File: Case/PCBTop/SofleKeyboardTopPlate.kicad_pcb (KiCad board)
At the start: 2 copper layers, 137.2 x 109.2 mm, 5 parts

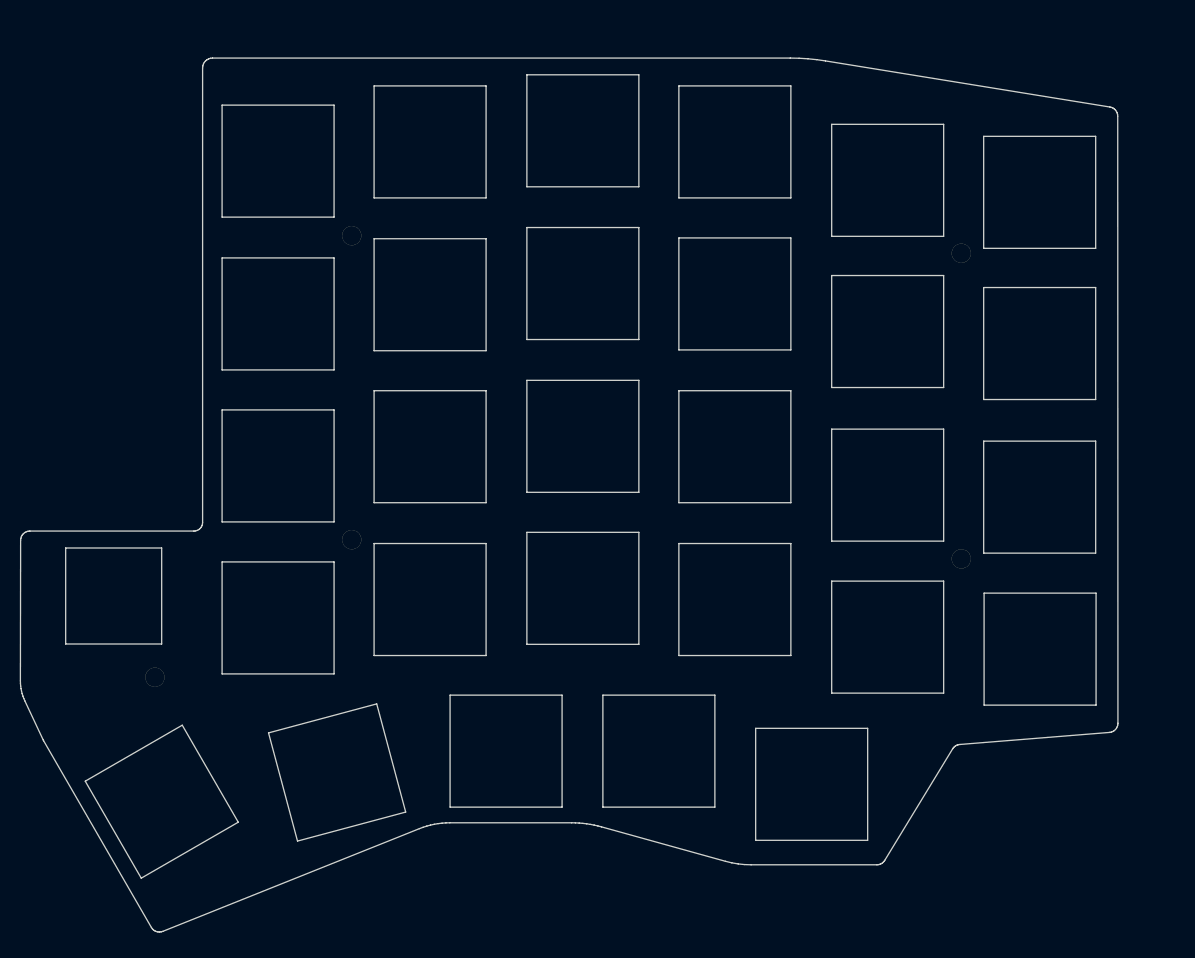
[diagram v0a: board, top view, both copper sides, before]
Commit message: Bottom case in kicad
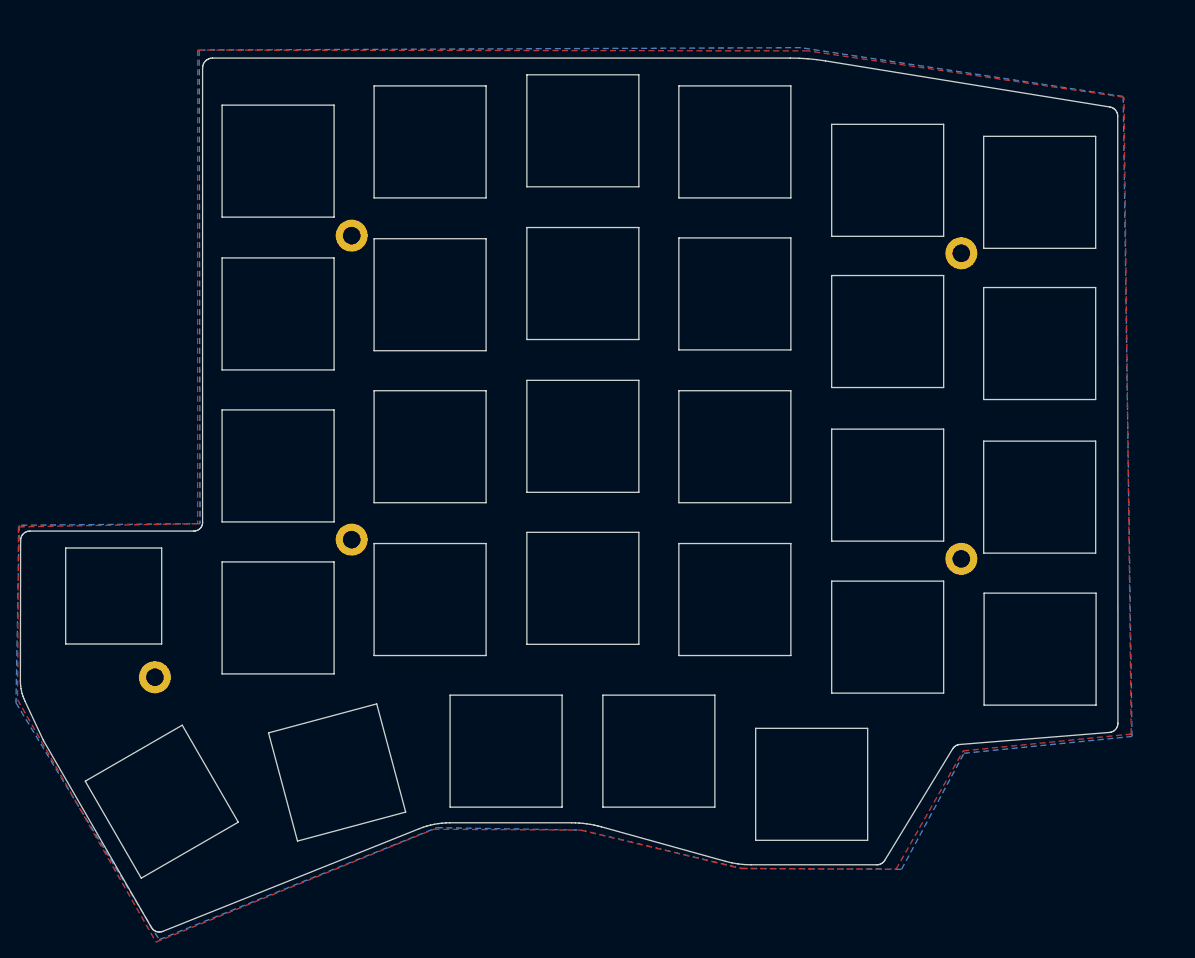
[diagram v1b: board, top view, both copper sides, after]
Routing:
- added copper zone on B.Cu, net (none)
- added copper zone on F.Cu, net (none)
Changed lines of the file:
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@@
     (mod_text_size 1 1)
     (mod_text_width 0.15)
-    (pad_size 1.524 1.524)
-    (pad_drill 0.762)
+    (pad_size 4 4)
+    (pad_drill 2.2)
     (pad_to_mask_clearance 0.2)
     (aux_axis_origin 0 0)
@@
       (effects (font (size 1.27 1.27) (thickness 0.15)))
     )
-    (pad 1 thru_hole circle (at 0 0) (size 2.4 2.4) (drill 2.4) (layers *.Cu *.Mask))
+    (pad 1 thru_hole circle (at 0 0) (size 4 4) (drill 2.2) (layers *.Cu *.Mask))
   )
   (module Wire_Pads:SolderWirePad_single_0-8mmDrill (layer F.Cu)
@@
       (effects (font (size 1.27 1.27) (thickness 0.15)))
     )
-    (pad 2 thru_hole circle (at 0 0) (size 2.4 2.4) (drill 2.4) (layers *.Cu *.Mask))
+    (pad 2 thru_hole circle (at 0 0) (size 4 4) (drill 2.2) (layers *.Cu *.Mask))
   )
   (module Wire_Pads:SolderWirePad_single_0-8mmDrill (layer F.Cu)
@@
       (effects (font (size 1.27 1.27) (thickness 0.15)))
     )
-    (pad 3 thru_hole circle (at 0 0) (size 2.4 2.4) (drill 2.4) (layers *.Cu *.Mask))
+    (pad 3 thru_hole circle (at 0 0) (size 4 4) (drill 2.2) (layers *.Cu *.Mask))
   )
   (module Wire_Pads:SolderWirePad_single_0-8mmDrill (layer F.Cu)
@@
       (effects (font (size 1.27 1.27) (thickness 0.15)))
     )
-    (pad 4 thru_hole circle (at 0 0) (size 2.4 2.4) (drill 2.4) (layers *.Cu *.Mask))
+    (pad 4 thru_hole circle (at 0 0) (size 4 4) (drill 2.2) (layers *.Cu *.Mask))
   )
   (module Wire_Pads:SolderWirePad_single_0-8mmDrill (layer F.Cu)
@@
       (effects (font (size 1.27 1.27) (thickness 0.15)))
     )
-    (pad 5 thru_hole circle (at 0 0) (size 2.4 2.4) (drill 2.4) (layers *.Cu *.Mask))
+    (pad 5 thru_hole circle (at 0 0) (size 4 4) (drill 2.2) (layers *.Cu *.Mask))
   )
   (gr_line (start 56.15827 40.380817) (end 42.16033 40.380817) (layer Edge.Cuts) (width 0.1))
@@
   (gr_line (start 22.609664 93.73982) (end 22.609664 81.739825) (layer Edge.Cuts) (width 0.1))
   (gr_line (start 22.609664 81.739825) (end 22.609664 81.739825) (layer Edge.Cuts) (width 0.1))
+  (zone (net 0) (net_name "") (layer F.Cu) (hatch edge 0.508)
+    (connect_pads (clearance 0.508))
+    (min_thickness 0.254)
+    (fill yes (arc_segments 32) (thermal_gap 0.508) (thermal_bridge_width 0.508))
+    (polygon
+      (pts
+        (xy 39.1 19.5) (xy 39.1 78.7) (xy 16.7 79.1) (xy 16.6 100.7) (xy 33.9 131)
+        (xy 68.6 116.9) (xy 87 117) (xy 107 121.8) (xy 126.4 121.9) (xy 134.8 107.1)
+        (xy 155.8 105) (xy 154.9 25.4) (xy 115.4 19.6)
+      )
+    )
+  )
+  (zone (net 0) (net_name "") (layer B.Cu) (hatch edge 0.508)
+    (connect_pads (clearance 0.508))
+    (min_thickness 0.254)
+    (fill yes (arc_segments 32) (thermal_gap 0.508) (thermal_bridge_width 0.508))
+    (polygon
+      (pts
+        (xy 39.3 19.5) (xy 39.4 78.7) (xy 16.8 78.9) (xy 16.4 101.1) (xy 34.3 130.7)
+        (xy 69 116.7) (xy 87 117) (xy 107.1 121.8) (xy 127.1 121.9) (xy 134.9 107.4)
+        (xy 155.9 105.3) (xy 154.8 25.3) (xy 114.5 19.2)
+      )
+    )
+  )
 )

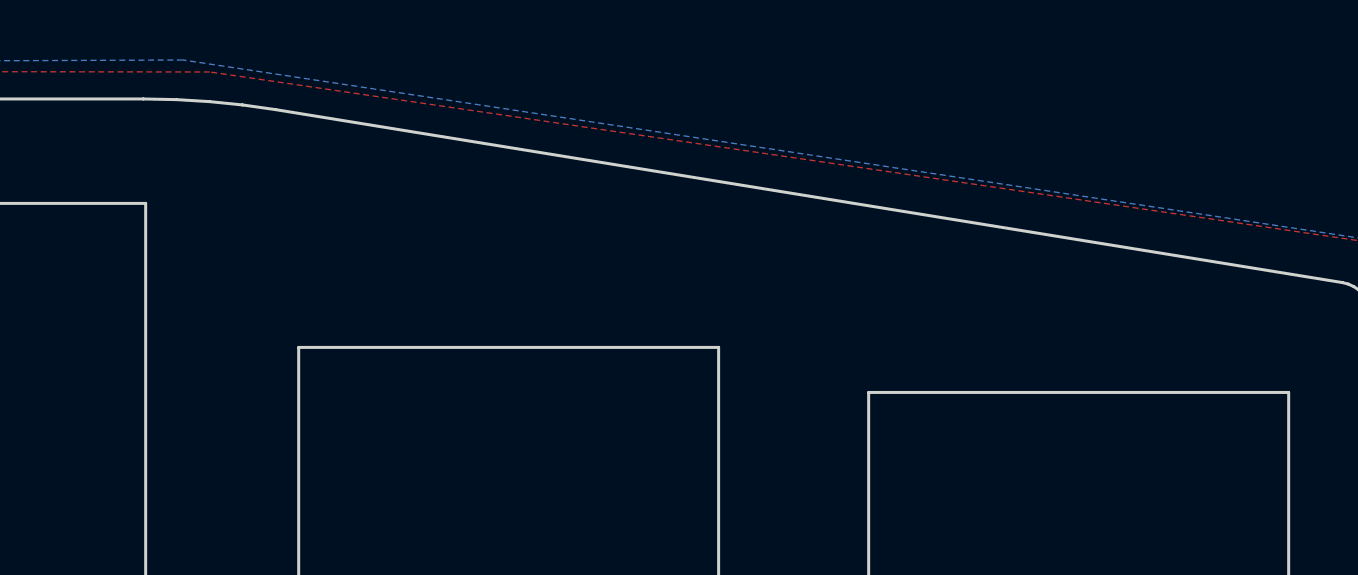
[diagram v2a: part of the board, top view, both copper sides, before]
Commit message: Finish top case
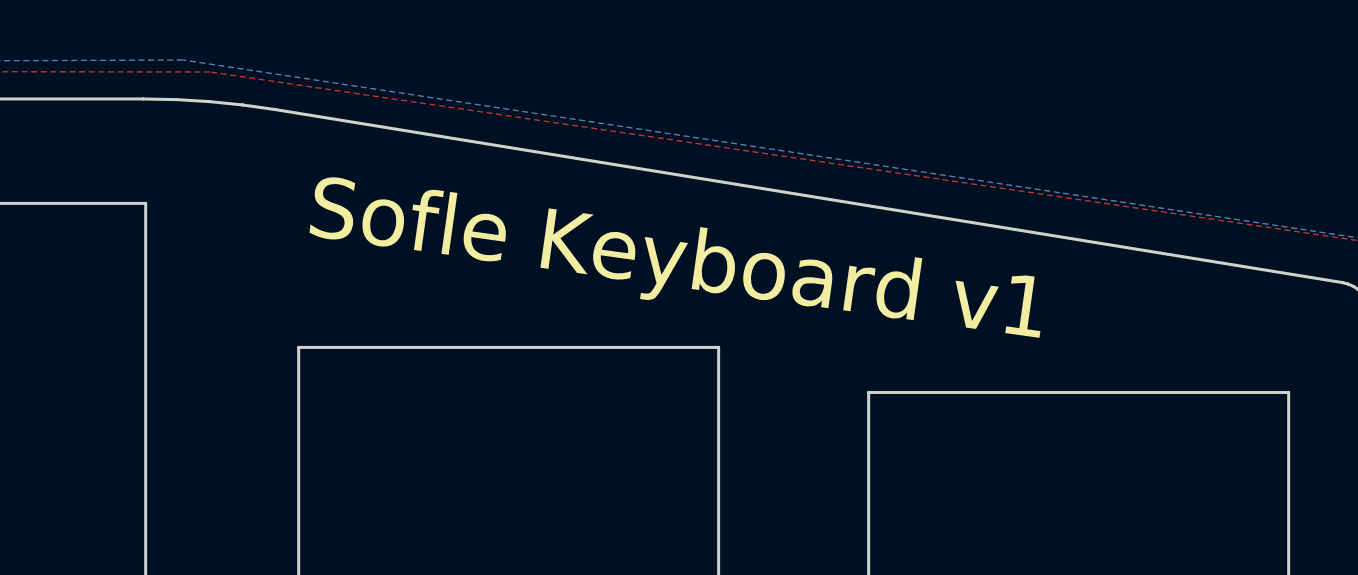
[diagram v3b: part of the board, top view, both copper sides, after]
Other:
- board text added: "Sofle Keyboard v1"
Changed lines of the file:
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@@
   (general
     (thickness 1.6)
-    (drawings 350)
+    (drawings 352)
     (tracks 0)
     (zones 0)
@@
     (visible_elements FFFFFF7F)
     (pcbplotparams
-      (layerselection 0x010f0_80000001)
+      (layerselection 0x010f0_ffffffff)
       (usegerberextensions false)
       (usegerberattributes false)
@@
       (outputformat 1)
       (mirror false)
-      (drillshape 1)
+      (drillshape 0)
       (scaleselection 1)
       (outputdirectory "gerbers/"))
@@
     (pad 5 thru_hole circle (at 0 0) (size 4 4) (drill 2.2) (layers *.Cu *.Mask Dwgs.User))
   )
+  (gr_text "Sofle Keyboard v1" (at 130.64 25.72 -8) (layer B.SilkS)
+    (effects (font (size 2 2) (thickness 0.3)) (justify mirror))
+  )
+  (gr_text "Sofle Keyboard v1" (at 131.04 25.84 -8) (layer F.SilkS)
+    (effects (font (size 2 2) (thickness 0.3)))
+  )
   (gr_line (start 56.15827 40.380817) (end 42.16033 40.380817) (layer Edge.Cuts) (width 0.1))

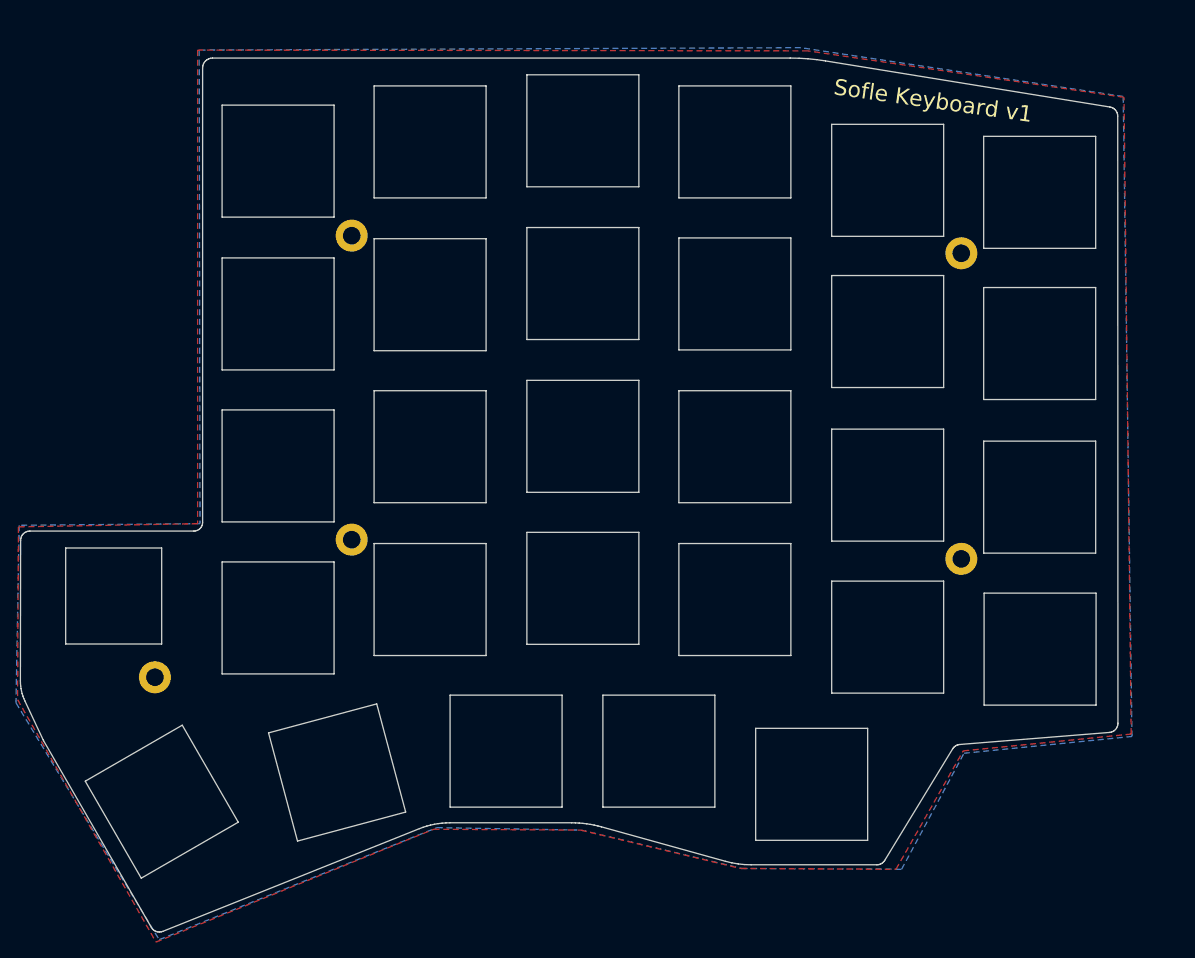
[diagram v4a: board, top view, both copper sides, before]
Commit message: Fix cutout for encoder (too small for build with choc switches).
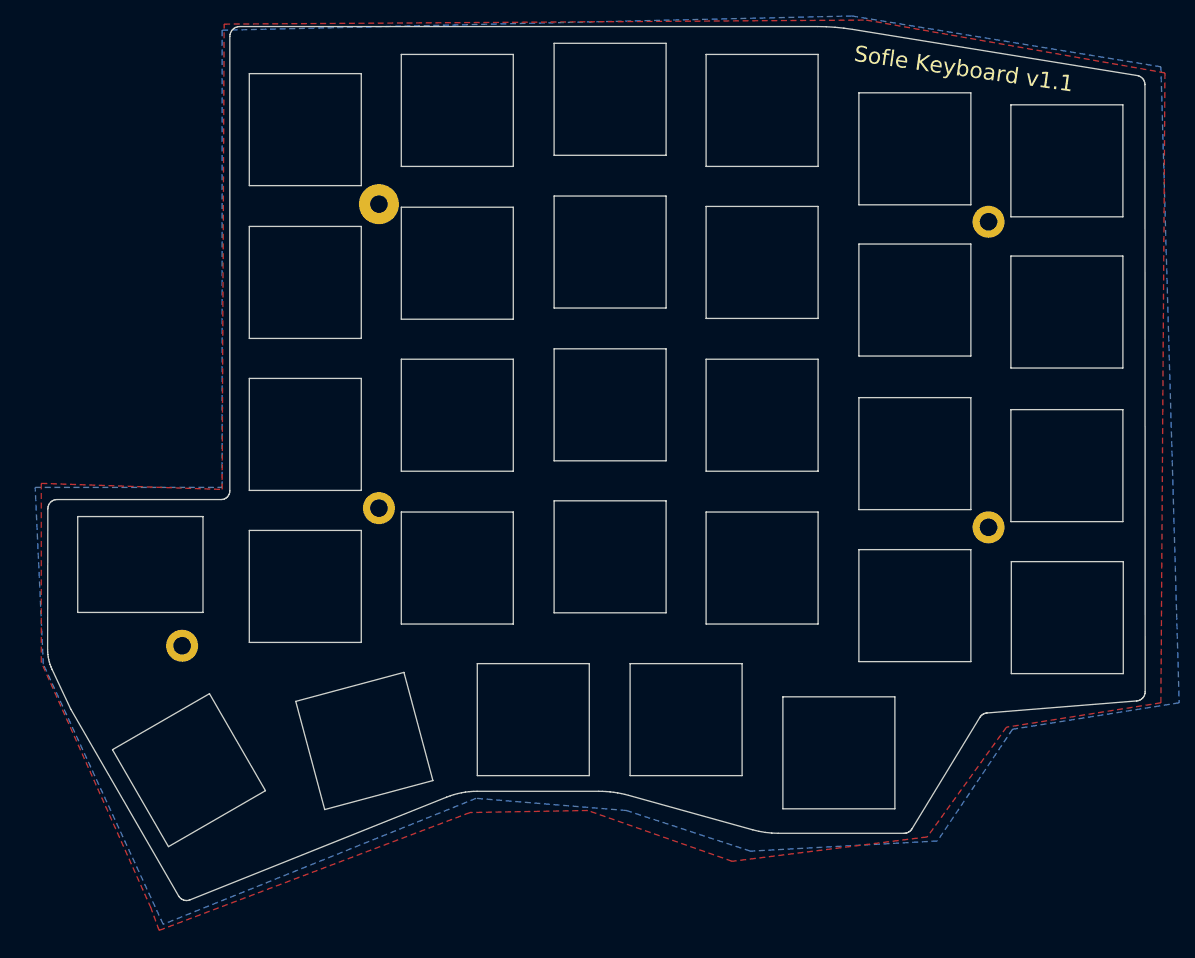
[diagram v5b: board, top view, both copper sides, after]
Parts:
- removed the ? at (58.4, 42.7)
- removed the ? at (58.4, 80.7)
- removed the ? at (33.8, 97.9)
- removed the ? at (134.6, 83.1)
- removed the ? at (134.6, 44.9)
- added ?: , Wire_Pads:SolderWirePad_single_0-8mmDrill, F.Cu at (61.8, 38.8)
- added ?: , Wire_Pads:SolderWirePad_single_0-8mmDrill, F.Cu at (61.8, 76.8)
- added ?: , Wire_Pads:SolderWirePad_single_0-8mmDrill, F.Cu at (37.2, 94.0)
- added ?: , Wire_Pads:SolderWirePad_single_0-8mmDrill, F.Cu at (138.0, 79.2)
- added ?: , Wire_Pads:SolderWirePad_single_0-8mmDrill, F.Cu at (138.0, 41.0)
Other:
- outline, holes or cut-outs redrawn
- board text added: "Sofle Keyboard v1.1"
- board text removed: "Sofle Keyboard v1"
